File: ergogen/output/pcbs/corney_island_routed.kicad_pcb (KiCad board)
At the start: 2 copper layers, 133.8 x 91.7 mm, 73 parts

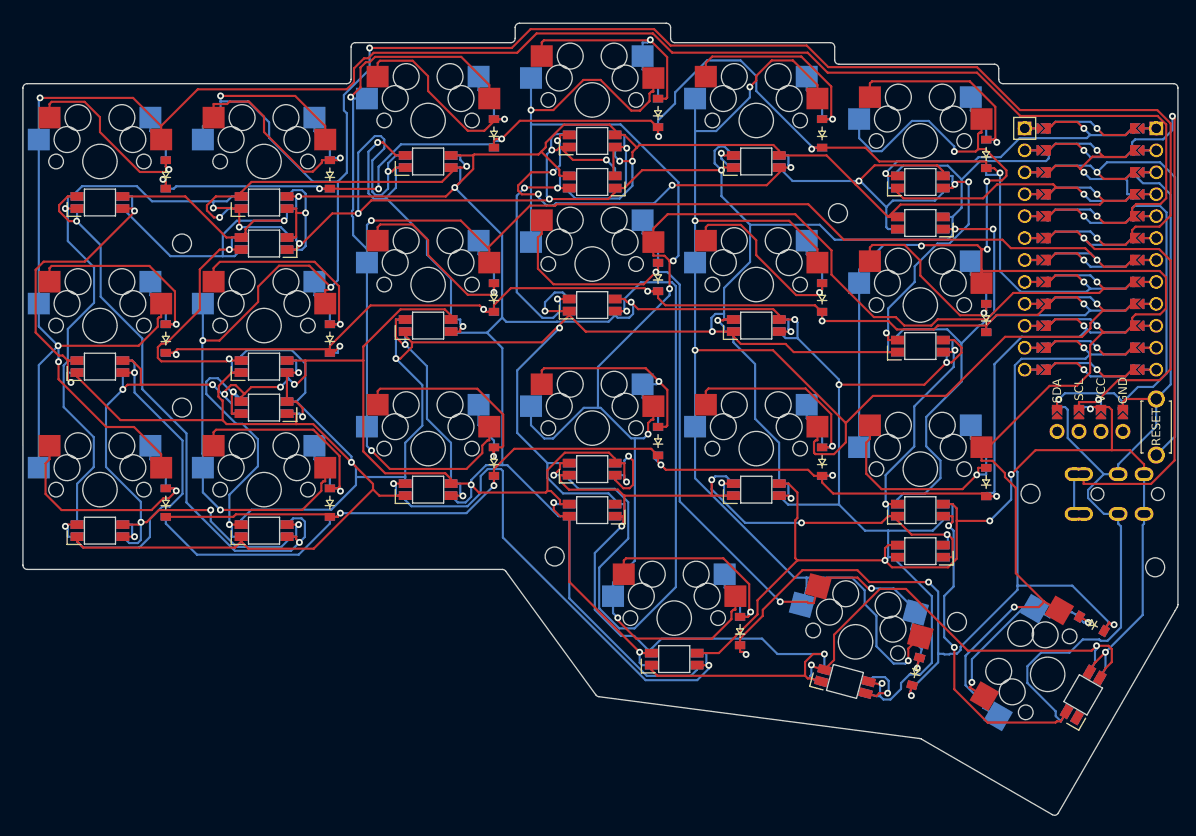
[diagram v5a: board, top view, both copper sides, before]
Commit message: Split diode position on F and B layers
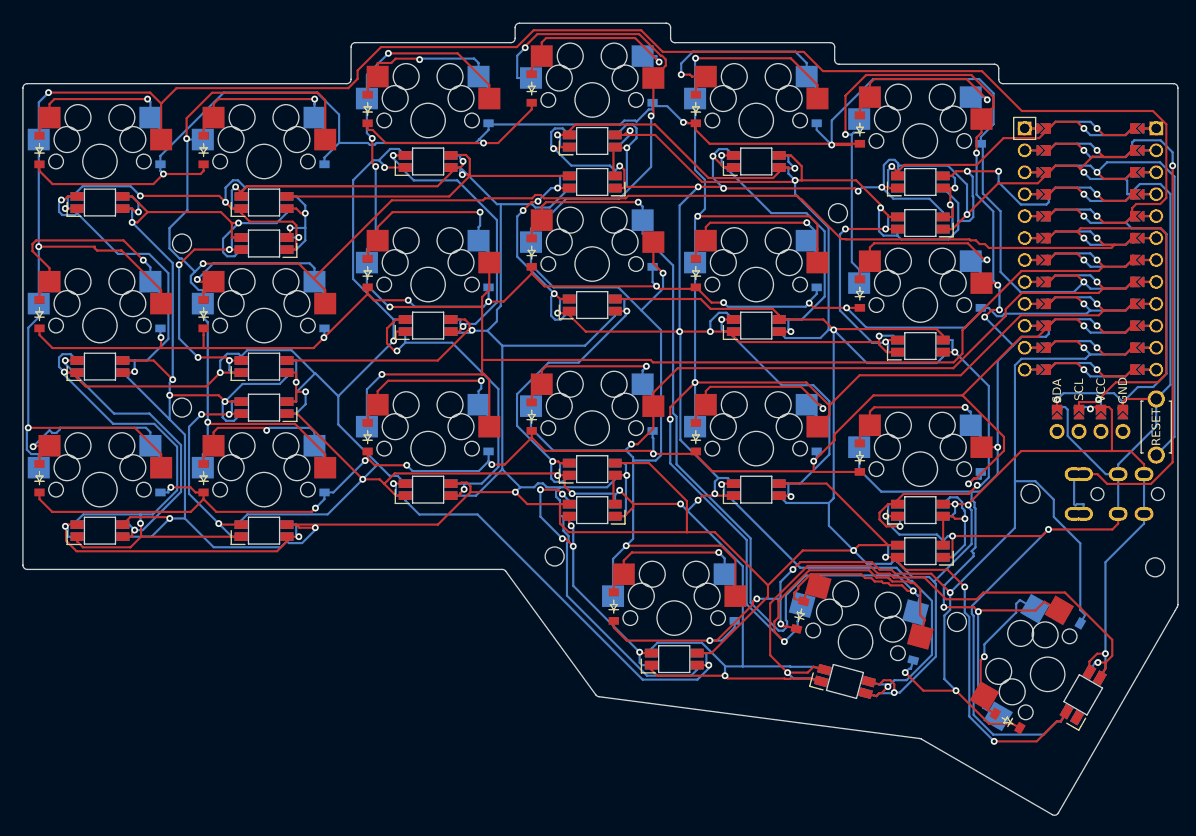
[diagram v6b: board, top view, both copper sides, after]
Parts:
- added D22: , ComboDiode, F.Cu at (93.0, 98.7)
- added D23: , ComboDiode, F.Cu at (93.0, 79.7)
- added D24: , ComboDiode, F.Cu at (93.0, 60.7)
- added D25: , ComboDiode, F.Cu at (112.0, 98.7)
- added D26: , ComboDiode, F.Cu at (112.0, 79.7)
- added D27: , ComboDiode, F.Cu at (112.0, 60.7)
- added D28: , ComboDiode, F.Cu at (131.0, 93.9)
- added D29: , ComboDiode, F.Cu at (131.0, 74.9)
- added D30: , ComboDiode, F.Cu at (131.0, 55.9)
- added D31: , ComboDiode, F.Cu at (150.0, 91.5)
- added D32: , ComboDiode, F.Cu at (150.0, 72.5)
- added D33: , ComboDiode, F.Cu at (150.0, 53.5)
- added D34: , ComboDiode, F.Cu at (169.0, 93.9)
- added D35: , ComboDiode, F.Cu at (169.0, 74.9)
- added D36: , ComboDiode, F.Cu at (169.0, 55.9)
- added D37: , ComboDiode, F.Cu at (188.0, 96.3)
- added D38: , ComboDiode, F.Cu at (188.0, 77.3)
- added D39: , ComboDiode, F.Cu at (188.0, 58.3)
- added D40: , ComboDiode, F.Cu at (159.5, 113.5)
- added D41: , ComboDiode, F.Cu at (181.1, 114.5)
- added D42: , ComboDiode, F.Cu at (205.1, 126.8)
- B1: footprint kbd:ResetSW -> corne_reset_switch
- moved D20 2.89 mm to (194.6, 118.2)
- moved D10 2.89 mm to (164.0, 91.5)
- moved D11 2.89 mm to (164.0, 72.5)
- moved D12 2.89 mm to (164.0, 53.5)
- moved D13 2.89 mm to (183.0, 93.9)
- moved D14 2.89 mm to (183.0, 74.9)
- moved D15 2.89 mm to (183.0, 55.9)
- moved D16 2.89 mm to (202.0, 96.3)
- moved D17 2.89 mm to (202.0, 77.3)
- moved D18 2.89 mm to (202.0, 58.3)
- moved D19 2.89 mm to (173.5, 113.5)
- moved D7 2.89 mm to (145.0, 93.9)
- moved D8 2.89 mm to (145.0, 74.9)
- moved D9 2.89 mm to (145.0, 55.9)
- moved D1 2.89 mm to (107.0, 98.7)
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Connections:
- LED1 pad 2: LED_21 -> LED_19
- LED1 pad 4: LED_20 -> LED_18
- LED10 pad 2: ULED_3 -> ULED_4
- LED12 pad 2: ULED_2 -> ULED_3
- LED13 pad 4: ULED_5 -> LED_5
- LED15 pad 4: ULED_6 -> LED_7
- LED16 pad 2: LED_3 -> ULED_2
- LED17 pad 4: LED_1 -> ULED_1
- LED22 pad 4: ULED_0 -> ULED_6
- LED23 pad 4: ULED_1 -> ULED_5
- LED24 pad 4: (no net) -> ULED_4
- LED25 pad 4: ULED_2 -> ULED_3
- LED26 pad 2: (no net) -> LED_3
- LED26 pad 4: (no net) -> ULED_2
- LED27 pad 2: (no net) -> ULED_1
- LED27 pad 4: (no net) -> LED_1
- LED3 pad 2: LED_19 -> LED_21
- LED3 pad 4: LED_18 -> LED_20
- LED5 pad 2: ULED_0 -> ULED_6
- LED6 pad 2: ULED_1 -> ULED_5
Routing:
- net GND: track 893.6 -> 752.5 mm, vias 25 -> 35
- net R0: track 159.8 -> 219.2 mm, vias 8 -> 5
- net LED_10: track 84.3 -> 37.0 mm
- net C1: track 258.5 -> 213.9 mm, vias 6 -> 4
- net LED_5: track 6.94 -> 50.9 mm, vias 1 -> 2
- net VCC: track 752.5 -> 791.2 mm, vias 27 -> 23
- net R3: track 121.7 -> 157.3 mm, vias 5 -> 8
- net LED_18: track 67.9 -> 36.6 mm
- net LED_7: track 3.96 -> 35.3 mm, vias 1 -> 2
- net LED_1: track 33.1 -> 12.6 mm, vias 3 -> 2
- net middle_home: track 101.6 -> 119.7 mm, vias 4 -> 2
- net LED_4: track 53.9 -> 70.7 mm
- net C4: track 203.1 -> 217.8 mm, vias 5 -> 6
- net R1: track 145.6 -> 159.6 mm, vias 6 -> 9
- net ULED_4: track 0.00 -> 13.4 mm, vias 0 -> 1
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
